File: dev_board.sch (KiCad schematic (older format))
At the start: 9 parts, among them J1 USB_B_Micro, J2 USB_A, J3 Conn_02x10_Odd_Even, J4 Conn_02x10_Odd_Even, SW1 SW_Push

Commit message: a bunch of stuff I guess. mostly layout.
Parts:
- removed C13: C_Small, symbol Device:C_Small
- removed J2: USB_A, symbol Connector:USB_A
- added C4, C5: 0.1uF, Capacitors_SMD:C_0603, symbol Device:C_Small
- added J2: ARJ-169, Exodus_Connectors:ARJ-169, symbol Exodus_Connectors:ARJ-169
- C2: renamed from C14; value C_Small -> 1uF; footprint (none) -> Capacitors_SMD:C_0603
- C3: renamed from C15; footprint (none) -> Capacitors_SMD:C_0603
- J1: footprint (none) -> Connectors_USB:USB_Micro-B_Molex-105017-0001
- R1: renamed from R13; value R_Small -> 10k; footprint (none) -> Resistors_SMD:R_0603
- SW1: footprint (none) -> Buttons_Switches_SMD:SW_SPST_EVPBF
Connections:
- net labels added: RXM, RXP, TXM, TXP
- wire segments 79 -> 104
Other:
- moved on the sheet: C2, C3, J3, J4, R1, SW1

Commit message: more layout
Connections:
- net RXM renamed RX_N
- net RXP renamed RX_P
- net TXM renamed TX_N
- net TXP renamed TX_P
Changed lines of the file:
@@
 	6800 2800 7150 2800
 Text Label 7000 2350 0    50   ~ 0
-RXM
+RX_N
 Text Label 7000 2450 0    50   ~ 0
-RXP
+RX_P
 Text Label 7000 2700 0    50   ~ 0
-TXM
+TX_N
 Text Label 7000 2800 0    50   ~ 0
-TXP
+TX_P
 $Comp
 L Exodus_Connectors:ARJ-169 J2

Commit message: layout
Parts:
- removed C2: 1uF, Capacitors_SMD:C_0603, symbol Device:C_Small
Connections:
- net stm32f107/OTG_FS_DM renamed stm32f107/OTG_FS_P
- net stm32f107/OTG_FS_DP renamed stm32f107/OTG_FS_N
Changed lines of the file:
@@
-	1    0    0    -1
-$EndComp
-$Comp
-L Device:C_Small C2
-U 1 1 5BB8F416
-P 2750 2950
-F 0 "C2" V 2550 2950 50  0000 C CNN
-F 1 "1uF" V 2650 3000 50  0000 C CNN
-F 2 "Capacitors_SMD:C_0603" H 2750 2950 50  0001 C CNN
-F 3 "~" H 2750 2950 50  0001 C CNN
-	1    2750 2950
-	0    1    1    0
-$EndComp
-$Comp
-L power:GND #PWR08
-U 1 1 5BB8F450
-P 2900 3000
-F 0 "#PWR08" H 2900 2750 50  0001 C CNN
-F 1 "GND" H 3000 3000 50  0000 C CNN
-F 2 "" H 2900 3000 50  0001 C CNN
-F 3 "" H 2900 3000 50  0001 C CNN
-	1    2900 3000
 	1    0    0    -1
 $EndComp
@@
 Wire Wire Line
 	2600 2800 2600 2950
-Connection ~ 2600 2950
-Wire Wire Line
-	2600 2950 2650 2950
-Wire Wire Line
-	2850 2950 2900 2950
-Wire Wire Line
-	2900 2950 2900 3000
 $Sheet
 S 3350 1800 1200 3450
@@
 F14 "JTDO" I L 3350 2250 50
 F15 "NJTRST" I L 3350 2450 50
-F16 "OTG_FS_DM" B L 3350 3250 50
-F17 "OTG_FS_DP" B L 3350 3150 50
-F18 "JTMS" I L 3350 2350 50
-F19 "PC2" I R 4550 3600 50
-F20 "PC3" I R 4550 3700 50
-F21 "PC6" I R 4550 3800 50
-F22 "PC7" I R 4550 3900 50
-F23 "PC8" I R 4550 4000 50
-F24 "PC10" I R 4550 4100 50
-F25 "PC11" I R 4550 4200 50
-F26 "PC12" I R 4550 4300 50
-F27 "PC13" I R 4550 4400 50
-F28 "PC14" I R 4550 4500 50
-F29 "PC15" I R 4550 4600 50
-F30 "PC0" I R 4550 3500 50
-F31 "PD2" I R 4550 4750 50
-F32 "PA0" B L 3350 3500 50
-F33 "PA1" I L 3350 3600 50
-F34 "PA3" I L 3350 3700 50
-F35 "PA4" I L 3350 3800 50
-F36 "PA5" I L 3350 3900 50
-F37 "PA6" I L 3350 4000 50
-F38 "PB0" I L 3350 4150 50
-F39 "PB1" I L 3350 4250 50
-F40 "PB2" I L 3350 4350 50
-F41 "PB5" I L 3350 4450 50
-F42 "PB6" I L 3350 4550 50
-F43 "PB7" I L 3350 4650 50
-F44 "PB8" I L 3350 4750 50
-F45 "PB9" I L 3350 4850 50
-F46 "PB10" I L 3350 4950 50
-F47 "PB14" I L 3350 5050 50
-F48 "PB15" I L 3350 5150 50
-F49 "PHY_INTRP" I R 4550 1950 50
+F16 "JTMS" I L 3350 2350 50
+F17 "PC2" I R 4550 3600 50
+F18 "PC3" I R 4550 3700 50
+F19 "PC6" I R 4550 3800 50
+F20 "PC7" I R 4550 3900 50
+F21 "PC8" I R 4550 4000 50
+F22 "PC10" I R 4550 4100 50
+F23 "PC11" I R 4550 4200 50
+F24 "PC12" I R 4550 4300 50
+F25 "PC13" I R 4550 4400 50
+F26 "PC14" I R 4550 4500 50
+F27 "PC15" I R 4550 4600 50
+F28 "PC0" I R 4550 3500 50
+F29 "PD2" I R 4550 4750 50
+F30 "PA0" B L 3350 3500 50
+F31 "PA1" I L 3350 3600 50
+F32 "PA3" I L 3350 3700 50
+F33 "PA4" I L 3350 3800 50
+F34 "PA5" I L 3350 3900 50
+F35 "PA6" I L 3350 4000 50
+F36 "PB0" I L 3350 4150 50
+F37 "PB1" I L 3350 4250 50
+F38 "PB2" I L 3350 4350 50
+F39 "PB5" I L 3350 4450 50
+F40 "PB6" I L 3350 4550 50
+F41 "PB7" I L 3350 4650 50
+F42 "PB8" I L 3350 4750 50
+F43 "PB9" I L 3350 4850 50
+F44 "PB10" I L 3350 4950 50
+F45 "PB14" I L 3350 5050 50
+F46 "PB15" I L 3350 5150 50
+F47 "PHY_INTRP" I R 4550 1950 50
+F48 "OTG_FS_N" B L 3350 3150 50
+F49 "OTG_FS_P" B L 3350 3250 50
 $EndSheet
-Wire Wire Line
-	2500 3150 3350 3150
-Wire Wire Line
-	2500 3250 3350 3250
 Wire Wire Line
 	1300 2500 1300 2550
@@
 Wire Wire Line
 	1750 1850 1750 1900
+Wire Wire Line
+	2500 3150 3350 3150
+Wire Wire Line
+	2500 3250 3350 3250
 $EndSCHEMATC

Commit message: updated power supply circuit. Better bandwidth, added softstart cap
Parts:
- J2: footprint (none) -> Exodus_Connectors:ARJ-169
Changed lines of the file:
@@
 F 0 "J2" H 2200 2728 50  0000 C CNN
 F 1 "ARJ-169" H 2200 2637 50  0000 C CNN
-F 2 "" H 2350 3750 50  0001 C CNN
+F 2 "Exodus_Connectors:ARJ-169" H 2350 3750 50  0001 C CNN
 F 3 "" H 2350 3750 50  0001 C CNN
 	2    2200 3150

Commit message: pcb updates or something
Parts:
- added D1: LED, LEDs:LED_0603, symbol Device:LED
- added R17, R18, R19: R, Resistors_SMD:R_0603, symbol Device:R
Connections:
- net +3V3: now also D1.2 (A)
- net +5V: no longer J1.1 (VBUS)
- net GND: now also J2.13, J2.15, R17.1
- net ethernet_phy_ksz8081/LED0: now also R18.2
- net at J2.14: now also R18.1
- net at J2.16: now also R19.1
- new net: D1.1 (K), R17.2
- new net LED1: R19.2
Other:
- moved on the sheet: C3, C4, C5, J1, J2A, J2B, J3, J4, R1, SW1

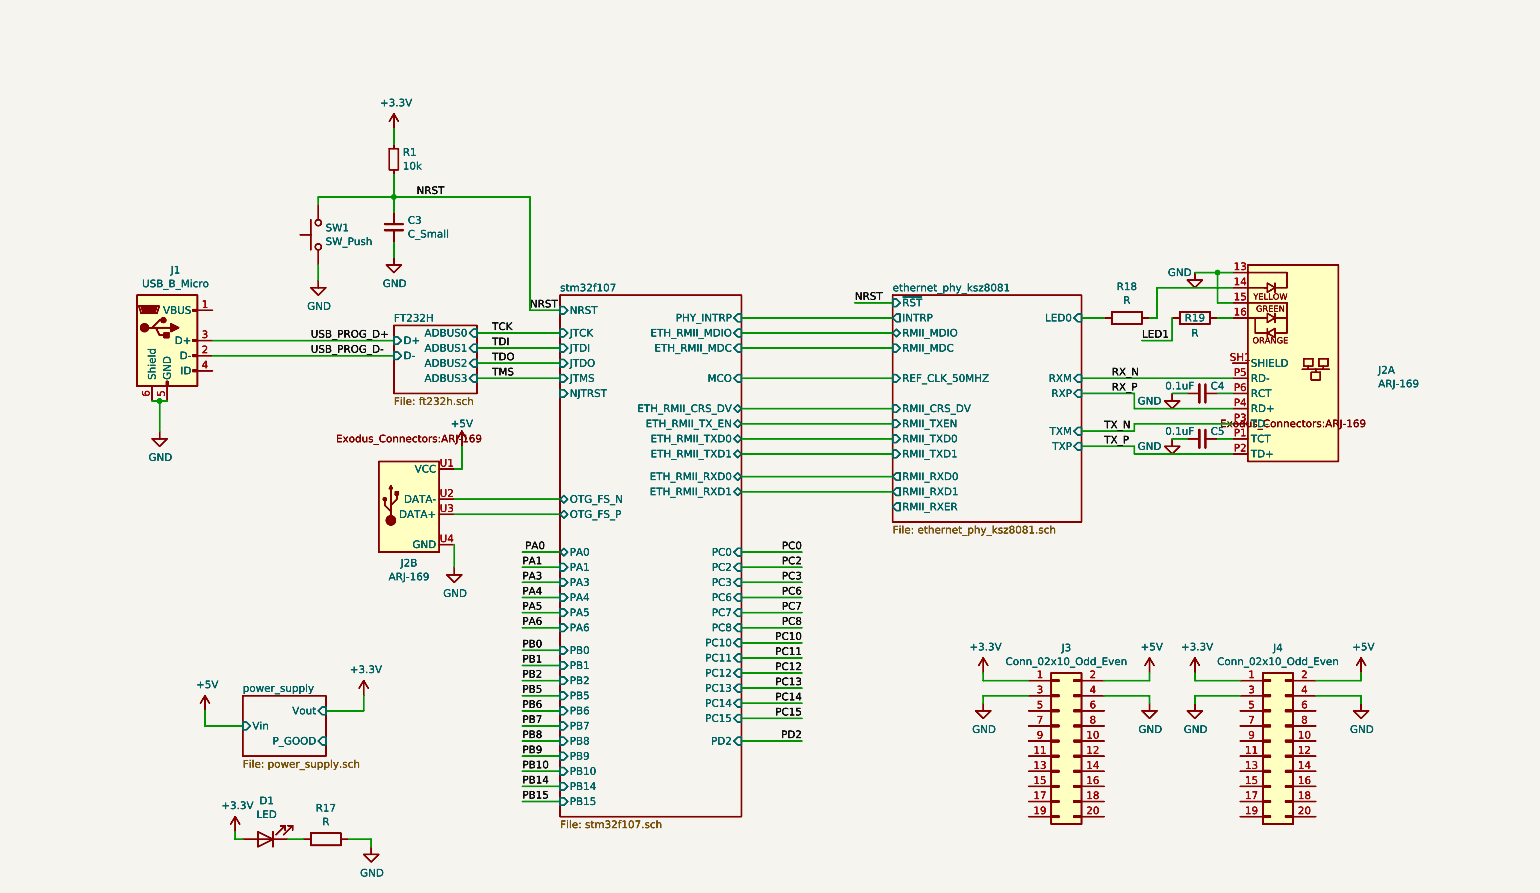
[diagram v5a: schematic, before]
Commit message: revised ethernet layout
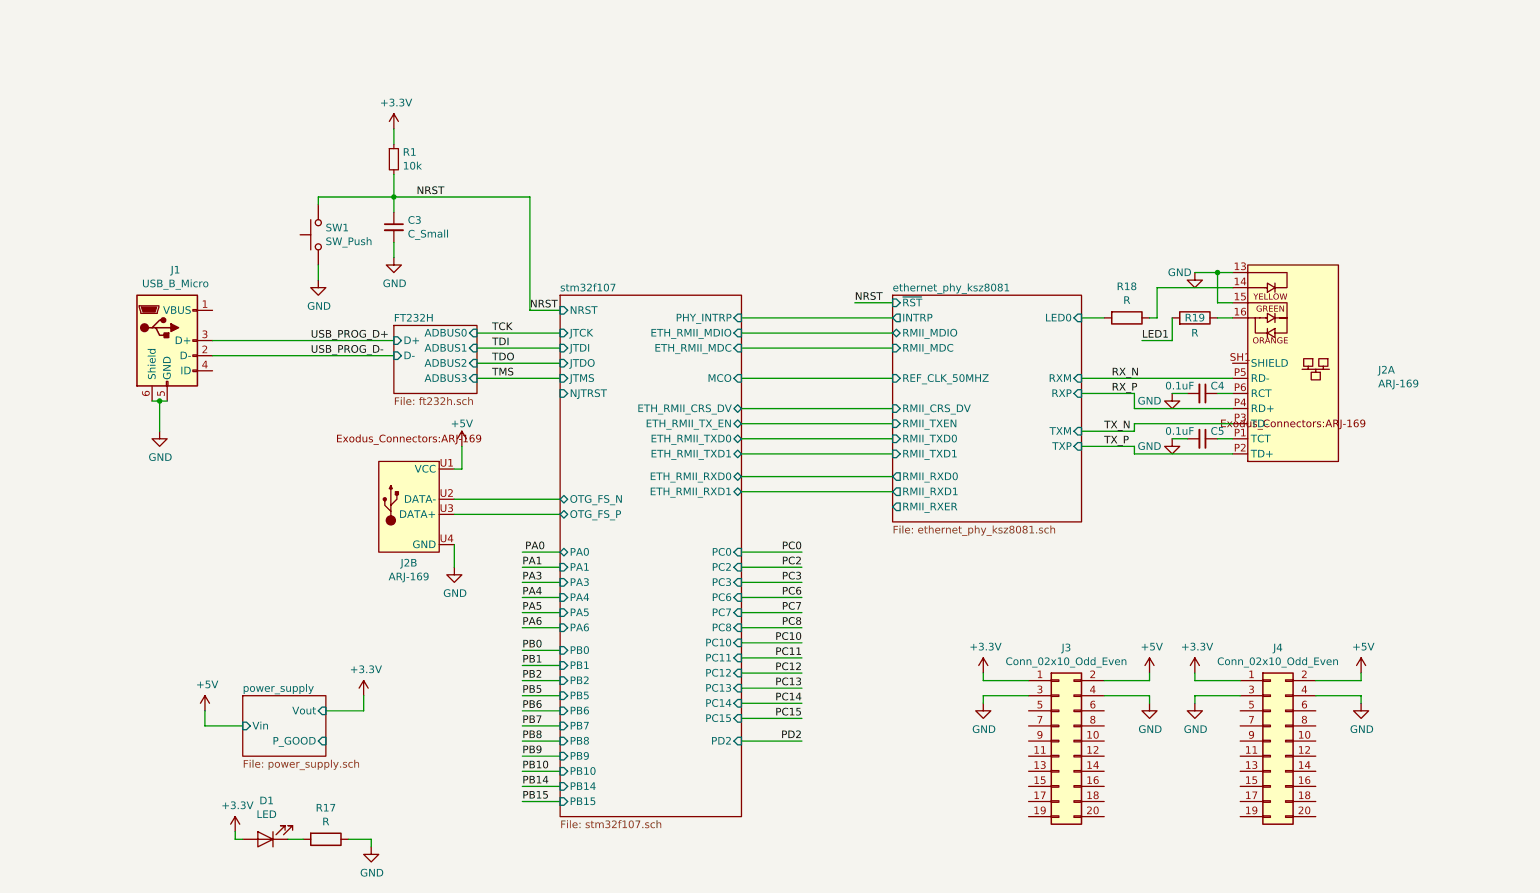
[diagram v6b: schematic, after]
